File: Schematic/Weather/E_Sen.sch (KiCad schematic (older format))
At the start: 27 parts, among them J6 3_Way_Wire, J7 3_Way_Wire, Q7 BSS138, Q8 AO3401, Q9 AO3401, U7 LM321

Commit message: more changes
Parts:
- renumbered C6 to C3, H9 to H11, H10 to H12, H11 to H13, H12 to H14, J6 to J19, J7 to J20, R31 to R29, R32 to R30, R33 to R31, R34 to R32, R35 to R33, R36 to R34, R37 to R35, R38 to R36, R39 to R37, R40 to R38, R41 to R39, R42 to R40, R43 to R41, R44 to R42, U7 to U6
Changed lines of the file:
@@
 $Descr A4 11693 8268
 encoding utf-8
-Sheet 12 14
+Sheet 12 15
 Title ""
 Date ""
@@
 P 6050 2100
 AR Path="/5C952539/5CAEF08F" Ref="U?"  Part="1"
-AR Path="/5CAC04D1/5CAEF08F" Ref="U7"  Part="1"
-F 0 "U7" H 6050 2581 50  0000 C CNN
+AR Path="/5CAC04D1/5CAEF08F" Ref="U6"  Part="1"
+F 0 "U6" H 6050 2581 50  0000 C CNN
 F 1 "LM321" H 6050 2490 50  0000 C CNN
 F 2 "Package_TO_SOT_SMD:SOT-23-5" H 6050 2100 50  0001 C CNN
@@
 P 5450 4750
 AR Path="/5C952539/5CAEF095" Ref="R?"  Part="1"
-AR Path="/5CAC04D1/5CAEF095" Ref="R31"  Part="1"
-F 0 "R31" V 5243 4750 50  0000 C CNN
+AR Path="/5CAC04D1/5CAEF095" Ref="R29"  Part="1"
+F 0 "R29" V 5243 4750 50  0000 C CNN
 F 1 "2.2K" V 5334 4750 50  0000 C CNN
 F 2 "Resistor_THT:R_Axial_DIN0204_L3.6mm_D1.6mm_P2.54mm_Vertical" V 5380 4750 50  0001 C CNN
@@
 P 5850 5200
 AR Path="/5C952539/5CAEF09B" Ref="R?"  Part="1"
-AR Path="/5CAC04D1/5CAEF09B" Ref="R34"  Part="1"
-F 0 "R34" H 5780 5154 50  0000 R CNN
+AR Path="/5CAC04D1/5CAEF09B" Ref="R32"  Part="1"
+F 0 "R32" H 5780 5154 50  0000 R CNN
 F 1 "5.1K" H 5780 5245 50  0000 R CNN
 F 2 "Resistor_THT:R_Axial_DIN0204_L3.6mm_D1.6mm_P2.54mm_Vertical" V 5780 5200 50  0001 C CNN
@@
 P 7350 4850
 AR Path="/5C952539/5CAEF0A1" Ref="R?"  Part="1"
-AR Path="/5CAC04D1/5CAEF0A1" Ref="R42"  Part="1"
-F 0 "R42" H 7420 4896 50  0000 L CNN
+AR Path="/5CAC04D1/5CAEF0A1" Ref="R40"  Part="1"
+F 0 "R40" H 7420 4896 50  0000 L CNN
 F 1 "680" H 7420 4805 50  0000 L CNN
 F 2 "Resistor_THT:R_Axial_DIN0204_L3.6mm_D1.6mm_P2.54mm_Vertical" V 7280 4850 50  0001 C CNN
@@
 P 7050 3850
 AR Path="/5C952539/5CAEF0A7" Ref="R?"  Part="1"
-AR Path="/5CAC04D1/5CAEF0A7" Ref="R40"  Part="1"
-F 0 "R40" H 7120 3896 50  0000 L CNN
+AR Path="/5CAC04D1/5CAEF0A7" Ref="R38"  Part="1"
+F 0 "R38" H 7120 3896 50  0000 L CNN
 F 1 "20K" H 7120 3805 50  0000 L CNN
 F 2 "Resistor_THT:R_Axial_DIN0204_L3.6mm_D1.6mm_P2.54mm_Vertical" V 6980 3850 50  0001 C CNN
@@
 P 6300 4100
 AR Path="/5C952539/5CAEF0AD" Ref="R?"  Part="1"
-AR Path="/5CAC04D1/5CAEF0AD" Ref="R36"  Part="1"
-F 0 "R36" H 6370 4146 50  0000 L CNN
+AR Path="/5CAC04D1/5CAEF0AD" Ref="R34"  Part="1"
+F 0 "R34" H 6370 4146 50  0000 L CNN
 F 1 "10K" H 6370 4055 50  0000 L CNN
 F 2 "Resistor_THT:R_Axial_DIN0204_L3.6mm_D1.6mm_P2.54mm_Vertical" V 6230 4100 50  0001 C CNN
@@
 P 5750 3650
 AR Path="/5C952539/5CAEF0B3" Ref="R?"  Part="1"
-AR Path="/5CAC04D1/5CAEF0B3" Ref="R33"  Part="1"
-F 0 "R33" H 5820 3696 50  0000 L CNN
+AR Path="/5CAC04D1/5CAEF0B3" Ref="R31"  Part="1"
+F 0 "R31" H 5820 3696 50  0000 L CNN
 F 1 "2.2k" H 5820 3605 50  0000 L CNN
 F 2 "Resistor_THT:R_Axial_DIN0204_L3.6mm_D1.6mm_P2.54mm_Vertical" V 5680 3650 50  0001 C CNN
@@
 P 6400 1650
 AR Path="/5C952539/5CAEF0B9" Ref="R?"  Part="1"
-AR Path="/5CAC04D1/5CAEF0B9" Ref="R37"  Part="1"
-F 0 "R37" H 6470 1696 50  0000 L CNN
+AR Path="/5CAC04D1/5CAEF0B9" Ref="R35"  Part="1"
+F 0 "R35" H 6470 1696 50  0000 L CNN
 F 1 "4.7K" H 6470 1605 50  0000 L CNN
 F 2 "Resistor_THT:R_Axial_DIN0204_L3.6mm_D1.6mm_P2.54mm_Vertical" V 6330 1650 50  0001 C CNN
@@
 P 5500 2100
 AR Path="/5C952539/5CAEF0CB" Ref="R?"  Part="1"
-AR Path="/5CAC04D1/5CAEF0CB" Ref="R32"  Part="1"
-F 0 "R32" V 5293 2100 50  0000 C CNN
+AR Path="/5CAC04D1/5CAEF0CB" Ref="R30"  Part="1"
+F 0 "R30" V 5293 2100 50  0000 C CNN
 F 1 "4.7K" V 5384 2100 50  0000 C CNN
 F 2 "Resistor_THT:R_Axial_DIN0204_L3.6mm_D1.6mm_P2.54mm_Vertical" V 5430 2100 50  0001 C CNN
@@
 P 7050 4850
 AR Path="/5C952539/5CAEF0EB" Ref="R?"  Part="1"
-AR Path="/5CAC04D1/5CAEF0EB" Ref="R41"  Part="1"
-F 0 "R41" H 7120 4896 50  0000 L CNN
+AR Path="/5CAC04D1/5CAEF0EB" Ref="R39"  Part="1"
+F 0 "R39" H 7120 4896 50  0000 L CNN
 F 1 "20K" H 7120 4805 50  0000 L CNN
 F 2 "Resistor_THT:R_Axial_DIN0204_L3.6mm_D1.6mm_P2.54mm_Vertical" V 6980 4850 50  0001 C CNN
@@
 P 7750 2200
 AR Path="/5C952539/5CAEF0FB" Ref="R?"  Part="1"
-AR Path="/5CAC04D1/5CAEF0FB" Ref="R44"  Part="1"
-F 0 "R44" V 7543 2200 50  0000 C CNN
+AR Path="/5CAC04D1/5CAEF0FB" Ref="R42"  Part="1"
+F 0 "R42" V 7543 2200 50  0000 C CNN
 F 1 "3.3k" V 7634 2200 50  0000 C CNN
 F 2 "Resistor_THT:R_Axial_DIN0204_L3.6mm_D1.6mm_P2.54mm_Vertical" V 7680 2200 50  0001 C CNN
@@
 P 6400 2600
 AR Path="/5C952539/5CAEF102" Ref="R?"  Part="1"
-AR Path="/5CAC04D1/5CAEF102" Ref="R38"  Part="1"
-F 0 "R38" H 6470 2646 50  0000 L CNN
+AR Path="/5CAC04D1/5CAEF102" Ref="R36"  Part="1"
+F 0 "R36" H 6470 2646 50  0000 L CNN
 F 1 "4.7K" H 6470 2555 50  0000 L CNN
 F 2 "Resistor_THT:R_Axial_DIN0204_L3.6mm_D1.6mm_P2.54mm_Vertical" V 6330 2600 50  0001 C CNN
@@
 P 6900 2200
 AR Path="/5C952539/5CAEF11E" Ref="C?"  Part="1"
-AR Path="/5CAC04D1/5CAEF11E" Ref="C6"  Part="1"
-F 0 "C6" V 6648 2200 50  0000 C CNN
+AR Path="/5CAC04D1/5CAEF11E" Ref="C3"  Part="1"
+F 0 "C3" V 6648 2200 50  0000 C CNN
 F 1 "0.1uF" V 6739 2200 50  0000 C CNN
 F 2 "Capacitor_THT:C_Disc_D3.8mm_W2.6mm_P2.50mm" H 6938 2050 50  0001 C CNN
@@
 P 6600 2200
 AR Path="/5C952539/5CAEF128" Ref="R?"  Part="1"
-AR Path="/5CAC04D1/5CAEF128" Ref="R39"  Part="1"
-F 0 "R39" V 6393 2200 50  0000 C CNN
+AR Path="/5CAC04D1/5CAEF128" Ref="R37"  Part="1"
+F 0 "R37" V 6393 2200 50  0000 C CNN
 F 1 "4.7K" V 6484 2200 50  0000 C CNN
 F 2 "Resistor_THT:R_Axial_DIN0204_L3.6mm_D1.6mm_P2.54mm_Vertical" V 6530 2200 50  0001 C CNN
@@
 P 5900 2450
 AR Path="/5C952539/5CAEF134" Ref="R?"  Part="1"
-AR Path="/5CAC04D1/5CAEF134" Ref="R35"  Part="1"
-F 0 "R35" V 5693 2450 50  0000 C CNN
+AR Path="/5CAC04D1/5CAEF134" Ref="R33"  Part="1"
+F 0 "R33" V 5693 2450 50  0000 C CNN
 F 1 "4.7K" V 5784 2450 50  0000 C CNN
 F 2 "Resistor_THT:R_Axial_DIN0204_L3.6mm_D1.6mm_P2.54mm_Vertical" V 5830 2450 50  0001 C CNN
@@
 P 7700 3750
 AR Path="/5C952539/5CAEF14F" Ref="R?"  Part="1"
-AR Path="/5CAC04D1/5CAEF14F" Ref="R43"  Part="1"
-F 0 "R43" H 7770 3796 50  0000 L CNN
+AR Path="/5CAC04D1/5CAEF14F" Ref="R41"  Part="1"
+F 0 "R41" H 7770 3796 50  0000 L CNN
 F 1 "47K" H 7770 3705 50  0000 L CNN
 F 2 "Resistor_THT:R_Axial_DIN0204_L3.6mm_D1.6mm_P2.54mm_Vertical" V 7630 3750 50  0001 C CNN
@@
 P 3650 1950
 AR Path="/5C952539/5CAEF15D" Ref="J?"  Part="1"
-AR Path="/5CAC04D1/5CAEF15D" Ref="J7"  Part="1"
-F 0 "J7" H 3500 1550 50  0000 L CNN
+AR Path="/5CAC04D1/5CAEF15D" Ref="J20"  Part="1"
+F 0 "J20" H 3500 1550 50  0000 L CNN
 F 1 "3_Way_Wire" H 3450 1400 50  0000 L CNN
 F 2 "Connector_PinHeader_2.54mm:PinHeader_1x03_P2.54mm_Vertical" H 3650 1950 50  0001 C CNN
@@
 P 3600 3300
 AR Path="/5C952539/5CAEF168" Ref="J?"  Part="1"
-AR Path="/5CAC04D1/5CAEF168" Ref="J6"  Part="1"
-F 0 "J6" H 3500 2900 50  0000 L CNN
+AR Path="/5CAC04D1/5CAEF168" Ref="J19"  Part="1"
+F 0 "J19" H 3500 2900 50  0000 L CNN
 F 1 "3_Way_Wire" H 3450 2750 50  0000 L CNN
 F 2 "Connector_PinHeader_2.54mm:PinHeader_1x03_P2.54mm_Vertical" H 3600 3300 50  0001 C CNN
@@
 P 8350 3300
 AR Path="/5C952539/5CAEF181" Ref="H?"  Part="1"
-AR Path="/5CAC04D1/5CAEF181" Ref="H9"  Part="1"
-F 0 "H9" H 8450 3349 50  0000 L CNN
+AR Path="/5CAC04D1/5CAEF181" Ref="H11"  Part="1"
+F 0 "H11" H 8450 3349 50  0000 L CNN
 F 1 "MountingHole_Pad" H 8450 3258 50  0000 L CNN
 F 2 "Connector_Wire:SolderWirePad_1x01_Drill0.8mm" H 8350 3300 50  0001 C CNN
@@
 P 8350 3800
 AR Path="/5C952539/5CAEF187" Ref="H?"  Part="1"
-AR Path="/5CAC04D1/5CAEF187" Ref="H11"  Part="1"
-F 0 "H11" H 8450 3849 50  0000 L CNN
+AR Path="/5CAC04D1/5CAEF187" Ref="H13"  Part="1"
+F 0 "H13" H 8450 3849 50  0000 L CNN
 F 1 "MountingHole_Pad" H 8450 3758 50  0000 L CNN
 F 2 "Connector_Wire:SolderWirePad_1x01_Drill0.8mm" H 8350 3800 50  0001 C CNN
@@
 P 8350 3500
 AR Path="/5C952539/5CAEF18D" Ref="H?"  Part="1"
-AR Path="/5CAC04D1/5CAEF18D" Ref="H10"  Part="1"
-F 0 "H10" H 8250 3457 50  0000 R CNN
+AR Path="/5CAC04D1/5CAEF18D" Ref="H12"  Part="1"
+F 0 "H12" H 8250 3457 50  0000 R CNN
 F 1 "MountingHole_Pad" H 8250 3548 50  0000 R CNN
 F 2 "Connector_Wire:SolderWirePad_1x01_Drill0.8mm" H 8350 3500 50  0001 C CNN
@@
 P 8350 4000
 AR Path="/5C952539/5CAEF194" Ref="H?"  Part="1"
-AR Path="/5CAC04D1/5CAEF194" Ref="H12"  Part="1"
-F 0 "H12" H 8250 3957 50  0000 R CNN
+AR Path="/5CAC04D1/5CAEF194" Ref="H14"  Part="1"
+F 0 "H14" H 8250 3957 50  0000 R CNN
 F 1 "MountingHole_Pad" H 8250 4048 50  0000 R CNN
 F 2 "Connector_Wire:SolderWirePad_1x01_Drill0.8mm" H 8350 4000 50  0001 C CNN

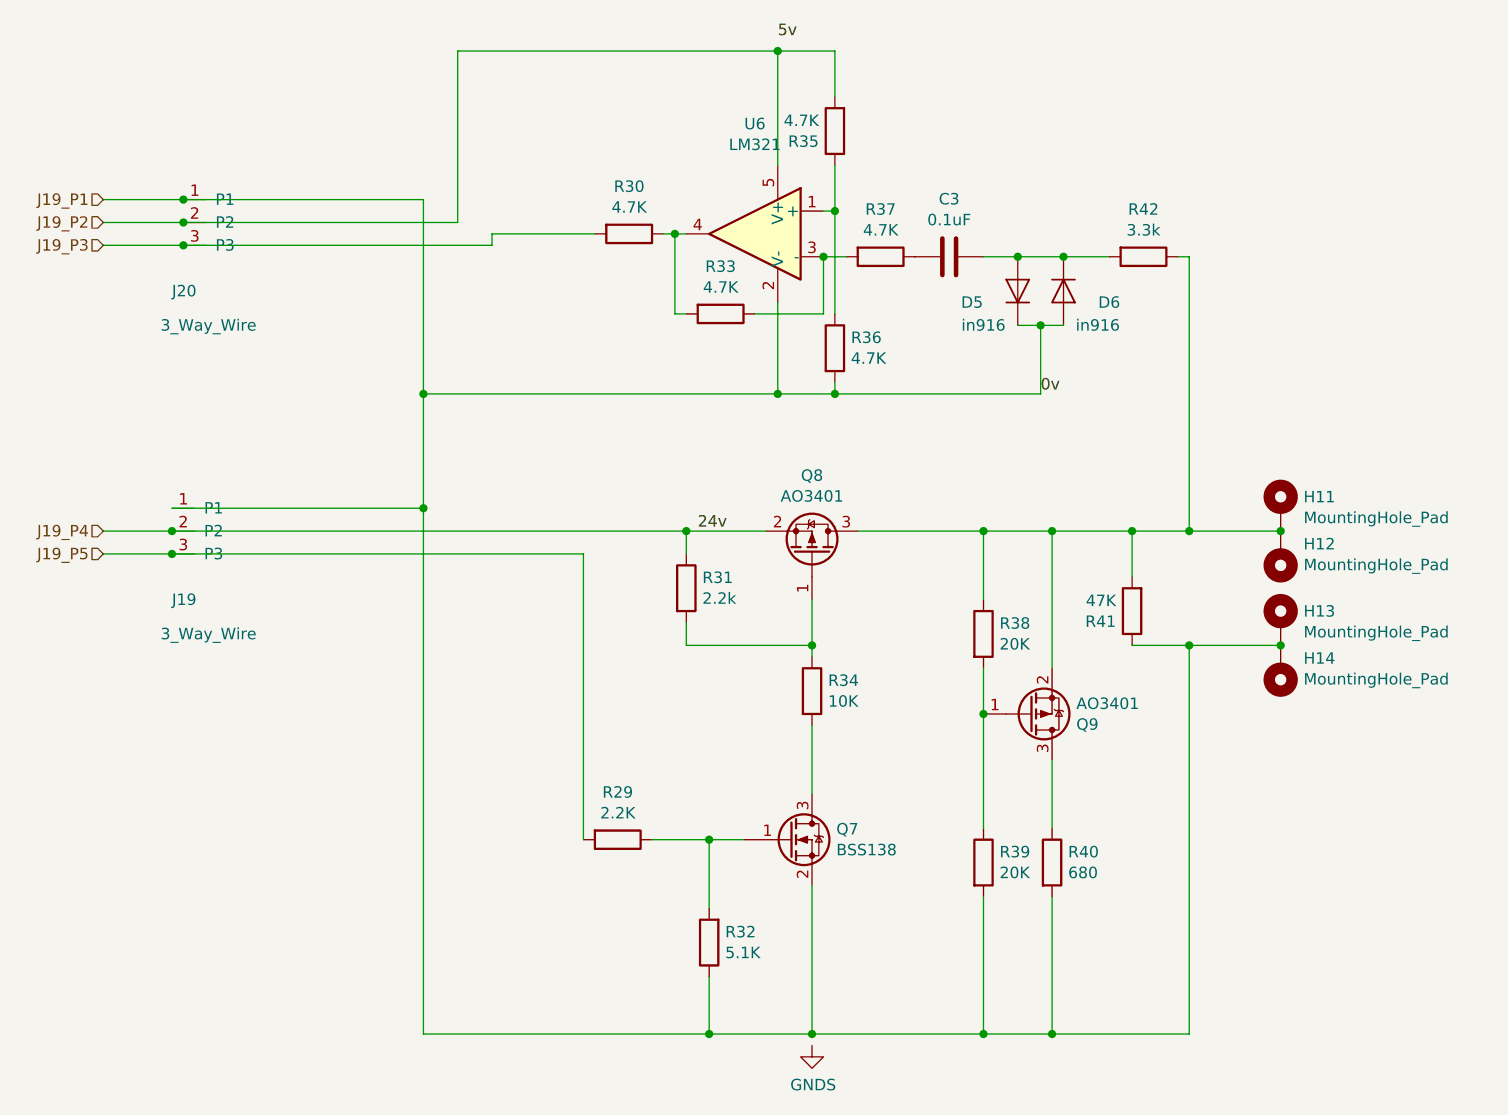
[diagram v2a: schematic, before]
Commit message: Connector relable start
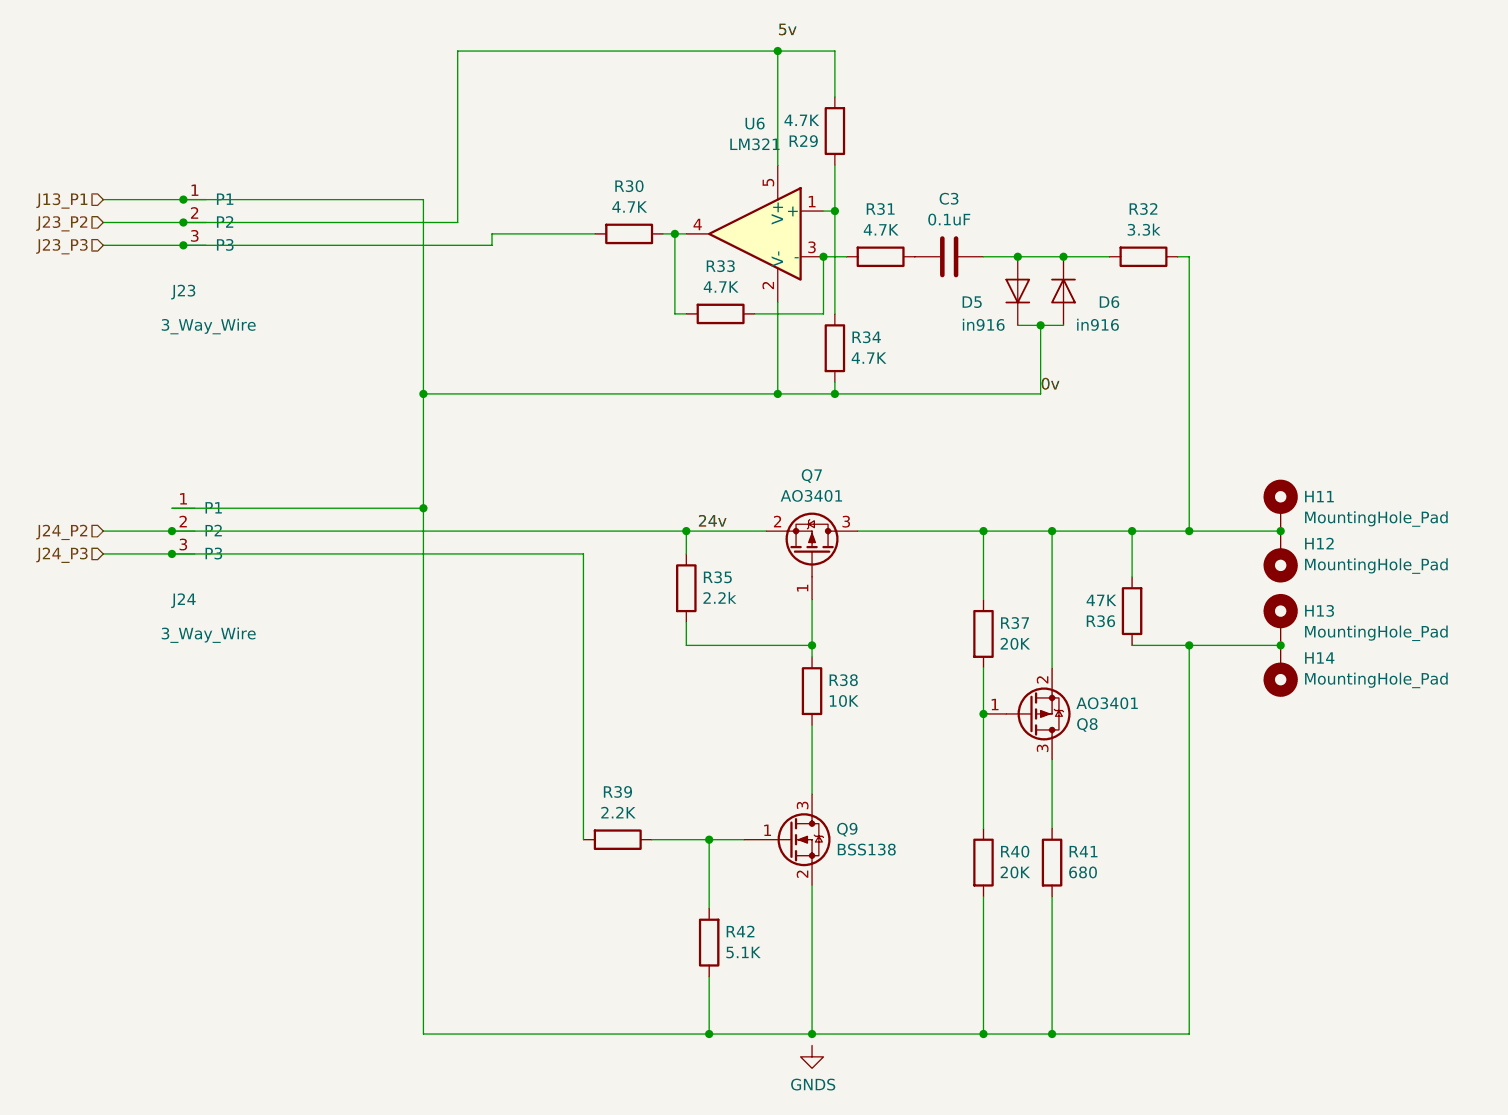
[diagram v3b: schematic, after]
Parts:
- renumbered J20 to J23, J19 to J24, Q8 to Q7, Q9 to Q8, Q7 to Q9, R35 to R29, R37 to R31, R42 to R32, R36 to R34, R31 to R35, R41 to R36, R38 to R37, R34 to R38, R29 to R39, R39 to R40, R40 to R41, R32 to R42
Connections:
- net J19_P1 renamed J13_P1
- net J19_P2 renamed J23_P2
- net J19_P3 renamed J23_P3
- net J19_P4 renamed J24_P2
- net J19_P5 renamed J24_P3
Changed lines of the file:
@@
 $Descr A4 11693 8268
 encoding utf-8
-Sheet 12 15
+Sheet 9 15
 Title ""
 Date ""
@@
 $EndDescr
 Text HLabel 3200 1950 0    50   Input ~ 0
-J19_P1
+J13_P1
 Text HLabel 3200 2050 0    50   Input ~ 0
-J19_P2
+J23_P2
 Text HLabel 3200 2150 0    50   Input ~ 0
-J19_P3
+J23_P3
 Text HLabel 3200 3400 0    50   Input ~ 0
-J19_P4
+J24_P2
 $Comp
 L Weather-rescue:AO3401-Transistor_FET Q?
@@
 P 6300 3500
 AR Path="/5C952539/5CAEF083" Ref="Q?"  Part="1"
-AR Path="/5CAC04D1/5CAEF083" Ref="Q8"  Part="1"
-F 0 "Q8" V 6643 3500 50  0000 C CNN
+AR Path="/5CAC04D1/5CAEF083" Ref="Q7"  Part="1"
+F 0 "Q7" V 6643 3500 50  0000 C CNN
 F 1 "AO3401" V 6552 3500 50  0000 C CNN
 F 2 "Package_TO_SOT_SMD:SOT-23" H 6500 3425 50  0001 L CIN
@@
 P 6200 4750
 AR Path="/5C952539/5CAEF089" Ref="Q?"  Part="1"
-AR Path="/5CAC04D1/5CAEF089" Ref="Q7"  Part="1"
-F 0 "Q7" H 6406 4796 50  0000 L CNN
+AR Path="/5CAC04D1/5CAEF089" Ref="Q9"  Part="1"
+F 0 "Q9" H 6406 4796 50  0000 L CNN
 F 1 "BSS138" H 6406 4705 50  0000 L CNN
 F 2 "Package_TO_SOT_SMD:SOT-23" H 6400 4675 50  0001 L CIN
@@
 P 5450 4750
 AR Path="/5C952539/5CAEF095" Ref="R?"  Part="1"
-AR Path="/5CAC04D1/5CAEF095" Ref="R29"  Part="1"
-F 0 "R29" V 5243 4750 50  0000 C CNN
+AR Path="/5CAC04D1/5CAEF095" Ref="R39"  Part="1"
+F 0 "R39" V 5243 4750 50  0000 C CNN
 F 1 "2.2K" V 5334 4750 50  0000 C CNN
 F 2 "Resistor_THT:R_Axial_DIN0204_L3.6mm_D1.6mm_P2.54mm_Vertical" V 5380 4750 50  0001 C CNN
@@
 P 5850 5200
 AR Path="/5C952539/5CAEF09B" Ref="R?"  Part="1"
-AR Path="/5CAC04D1/5CAEF09B" Ref="R32"  Part="1"
-F 0 "R32" H 5780 5154 50  0000 R CNN
+AR Path="/5CAC04D1/5CAEF09B" Ref="R42"  Part="1"
+F 0 "R42" H 5780 5154 50  0000 R CNN
 F 1 "5.1K" H 5780 5245 50  0000 R CNN
 F 2 "Resistor_THT:R_Axial_DIN0204_L3.6mm_D1.6mm_P2.54mm_Vertical" V 5780 5200 50  0001 C CNN
@@
 P 7350 4850
 AR Path="/5C952539/5CAEF0A1" Ref="R?"  Part="1"
-AR Path="/5CAC04D1/5CAEF0A1" Ref="R40"  Part="1"
-F 0 "R40" H 7420 4896 50  0000 L CNN
+AR Path="/5CAC04D1/5CAEF0A1" Ref="R41"  Part="1"
+F 0 "R41" H 7420 4896 50  0000 L CNN
 F 1 "680" H 7420 4805 50  0000 L CNN
 F 2 "Resistor_THT:R_Axial_DIN0204_L3.6mm_D1.6mm_P2.54mm_Vertical" V 7280 4850 50  0001 C CNN
@@
 P 7050 3850
 AR Path="/5C952539/5CAEF0A7" Ref="R?"  Part="1"
-AR Path="/5CAC04D1/5CAEF0A7" Ref="R38"  Part="1"
-F 0 "R38" H 7120 3896 50  0000 L CNN
+AR Path="/5CAC04D1/5CAEF0A7" Ref="R37"  Part="1"
+F 0 "R37" H 7120 3896 50  0000 L CNN
 F 1 "20K" H 7120 3805 50  0000 L CNN
 F 2 "Resistor_THT:R_Axial_DIN0204_L3.6mm_D1.6mm_P2.54mm_Vertical" V 6980 3850 50  0001 C CNN
@@
 P 6300 4100
 AR Path="/5C952539/5CAEF0AD" Ref="R?"  Part="1"
-AR Path="/5CAC04D1/5CAEF0AD" Ref="R34"  Part="1"
-F 0 "R34" H 6370 4146 50  0000 L CNN
+AR Path="/5CAC04D1/5CAEF0AD" Ref="R38"  Part="1"
+F 0 "R38" H 6370 4146 50  0000 L CNN
 F 1 "10K" H 6370 4055 50  0000 L CNN
 F 2 "Resistor_THT:R_Axial_DIN0204_L3.6mm_D1.6mm_P2.54mm_Vertical" V 6230 4100 50  0001 C CNN
@@
 P 5750 3650
 AR Path="/5C952539/5CAEF0B3" Ref="R?"  Part="1"
-AR Path="/5CAC04D1/5CAEF0B3" Ref="R31"  Part="1"
-F 0 "R31" H 5820 3696 50  0000 L CNN
+AR Path="/5CAC04D1/5CAEF0B3" Ref="R35"  Part="1"
+F 0 "R35" H 5820 3696 50  0000 L CNN
 F 1 "2.2k" H 5820 3605 50  0000 L CNN
 F 2 "Resistor_THT:R_Axial_DIN0204_L3.6mm_D1.6mm_P2.54mm_Vertical" V 5680 3650 50  0001 C CNN
@@
 P 6400 1650
 AR Path="/5C952539/5CAEF0B9" Ref="R?"  Part="1"
-AR Path="/5CAC04D1/5CAEF0B9" Ref="R35"  Part="1"
-F 0 "R35" H 6470 1696 50  0000 L CNN
+AR Path="/5CAC04D1/5CAEF0B9" Ref="R29"  Part="1"
+F 0 "R29" H 6470 1696 50  0000 L CNN
 F 1 "4.7K" H 6470 1605 50  0000 L CNN
 F 2 "Resistor_THT:R_Axial_DIN0204_L3.6mm_D1.6mm_P2.54mm_Vertical" V 6330 1650 50  0001 C CNN
@@
 P 7250 4200
 AR Path="/5C952539/5CAEF0E4" Ref="Q?"  Part="1"
-AR Path="/5CAC04D1/5CAEF0E4" Ref="Q9"  Part="1"
-F 0 "Q9" H 7456 4246 50  0000 L CNN
+AR Path="/5CAC04D1/5CAEF0E4" Ref="Q8"  Part="1"
+F 0 "Q8" H 7456 4246 50  0000 L CNN
 F 1 "AO3401" H 7456 4155 50  0000 L CNN
 F 2 "Package_TO_SOT_SMD:SOT-23" H 7450 4125 50  0001 L CIN
@@
 P 7050 4850
 AR Path="/5C952539/5CAEF0EB" Ref="R?"  Part="1"
-AR Path="/5CAC04D1/5CAEF0EB" Ref="R39"  Part="1"
-F 0 "R39" H 7120 4896 50  0000 L CNN
+AR Path="/5CAC04D1/5CAEF0EB" Ref="R40"  Part="1"
+F 0 "R40" H 7120 4896 50  0000 L CNN
 F 1 "20K" H 7120 4805 50  0000 L CNN
 F 2 "Resistor_THT:R_Axial_DIN0204_L3.6mm_D1.6mm_P2.54mm_Vertical" V 6980 4850 50  0001 C CNN
@@
 P 7750 2200
 AR Path="/5C952539/5CAEF0FB" Ref="R?"  Part="1"
-AR Path="/5CAC04D1/5CAEF0FB" Ref="R42"  Part="1"
-F 0 "R42" V 7543 2200 50  0000 C CNN
+AR Path="/5CAC04D1/5CAEF0FB" Ref="R32"  Part="1"
+F 0 "R32" V 7543 2200 50  0000 C CNN
 F 1 "3.3k" V 7634 2200 50  0000 C CNN
 F 2 "Resistor_THT:R_Axial_DIN0204_L3.6mm_D1.6mm_P2.54mm_Vertical" V 7680 2200 50  0001 C CNN
@@
 P 6400 2600
 AR Path="/5C952539/5CAEF102" Ref="R?"  Part="1"
-AR Path="/5CAC04D1/5CAEF102" Ref="R36"  Part="1"
-F 0 "R36" H 6470 2646 50  0000 L CNN
+AR Path="/5CAC04D1/5CAEF102" Ref="R34"  Part="1"
+F 0 "R34" H 6470 2646 50  0000 L CNN
 F 1 "4.7K" H 6470 2555 50  0000 L CNN
 F 2 "Resistor_THT:R_Axial_DIN0204_L3.6mm_D1.6mm_P2.54mm_Vertical" V 6330 2600 50  0001 C CNN
@@
 P 6600 2200
 AR Path="/5C952539/5CAEF128" Ref="R?"  Part="1"
-AR Path="/5CAC04D1/5CAEF128" Ref="R37"  Part="1"
-F 0 "R37" V 6393 2200 50  0000 C CNN
+AR Path="/5CAC04D1/5CAEF128" Ref="R31"  Part="1"
+F 0 "R31" V 6393 2200 50  0000 C CNN
 F 1 "4.7K" V 6484 2200 50  0000 C CNN
 F 2 "Resistor_THT:R_Axial_DIN0204_L3.6mm_D1.6mm_P2.54mm_Vertical" V 6530 2200 50  0001 C CNN
@@
 Connection ~ 6350 2200
 Text HLabel 3200 3500 0    50   Input ~ 0
-J19_P5
+J24_P3
 Wire Wire Line
 	5750 3800 5750 3900
@@
 P 7700 3750
 AR Path="/5C952539/5CAEF14F" Ref="R?"  Part="1"
-AR Path="/5CAC04D1/5CAEF14F" Ref="R41"  Part="1"
-F 0 "R41" H 7770 3796 50  0000 L CNN
+AR Path="/5CAC04D1/5CAEF14F" Ref="R36"  Part="1"
+F 0 "R36" H 7770 3796 50  0000 L CNN
 F 1 "47K" H 7770 3705 50  0000 L CNN
 F 2 "Resistor_THT:R_Axial_DIN0204_L3.6mm_D1.6mm_P2.54mm_Vertical" V 7630 3750 50  0001 C CNN
@@
 P 3650 1950
 AR Path="/5C952539/5CAEF15D" Ref="J?"  Part="1"
-AR Path="/5CAC04D1/5CAEF15D" Ref="J20"  Part="1"
-F 0 "J20" H 3500 1550 50  0000 L CNN
+AR Path="/5CAC04D1/5CAEF15D" Ref="J23"  Part="1"
+F 0 "J23" H 3500 1550 50  0000 L CNN
 F 1 "3_Way_Wire" H 3450 1400 50  0000 L CNN
 F 2 "Connector_PinHeader_2.54mm:PinHeader_1x03_P2.54mm_Vertical" H 3650 1950 50  0001 C CNN
@@
 P 3600 3300
 AR Path="/5C952539/5CAEF168" Ref="J?"  Part="1"
-AR Path="/5CAC04D1/5CAEF168" Ref="J19"  Part="1"
-F 0 "J19" H 3500 2900 50  0000 L CNN
+AR Path="/5CAC04D1/5CAEF168" Ref="J24"  Part="1"
+F 0 "J24" H 3500 2900 50  0000 L CNN
 F 1 "3_Way_Wire" H 3450 2750 50  0000 L CNN
 F 2 "Connector_PinHeader_2.54mm:PinHeader_1x03_P2.54mm_Vertical" H 3600 3300 50  0001 C CNN
